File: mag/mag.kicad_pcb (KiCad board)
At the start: 4 copper layers, 87 x 51 mm, 77 parts, among them K1 Кнопка_KLS7-TS5401-1.35-250-T, K2 Кнопка_KLS7-TS5401-1.35-250-T, X1 отверстие_под_пайку, X2 отверстие_под_пайку, X3 отверстие_под_пайку, X4 отверстие_под_пайку

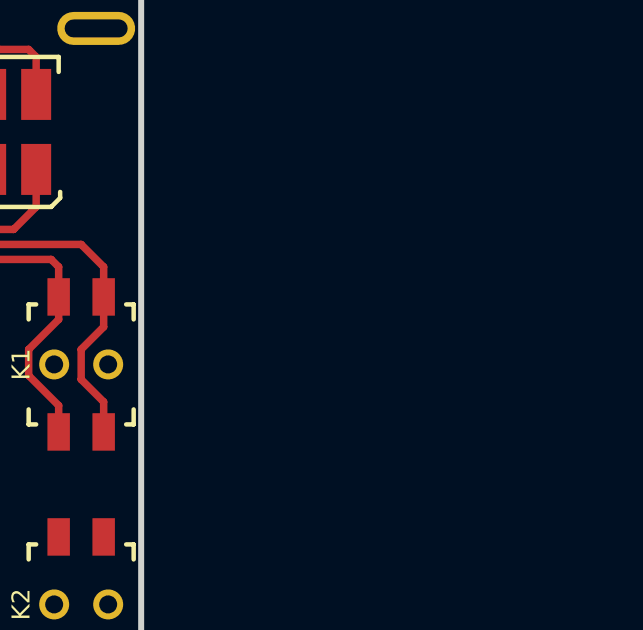
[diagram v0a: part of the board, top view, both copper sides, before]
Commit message: вынесен, но не подключен LDO на 2,5В
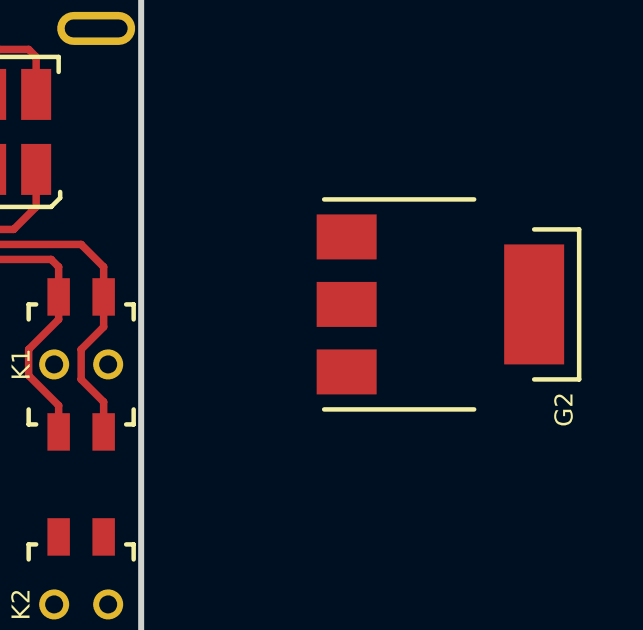
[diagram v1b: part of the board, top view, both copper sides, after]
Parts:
- added G2: Микросхема*LDO*IN8V*OUT2V5*1,2A*SOT-223, N_VD_HL:Транзистор_NPN_SOT223_pnp, F.Cu at (187.0, 87.8)

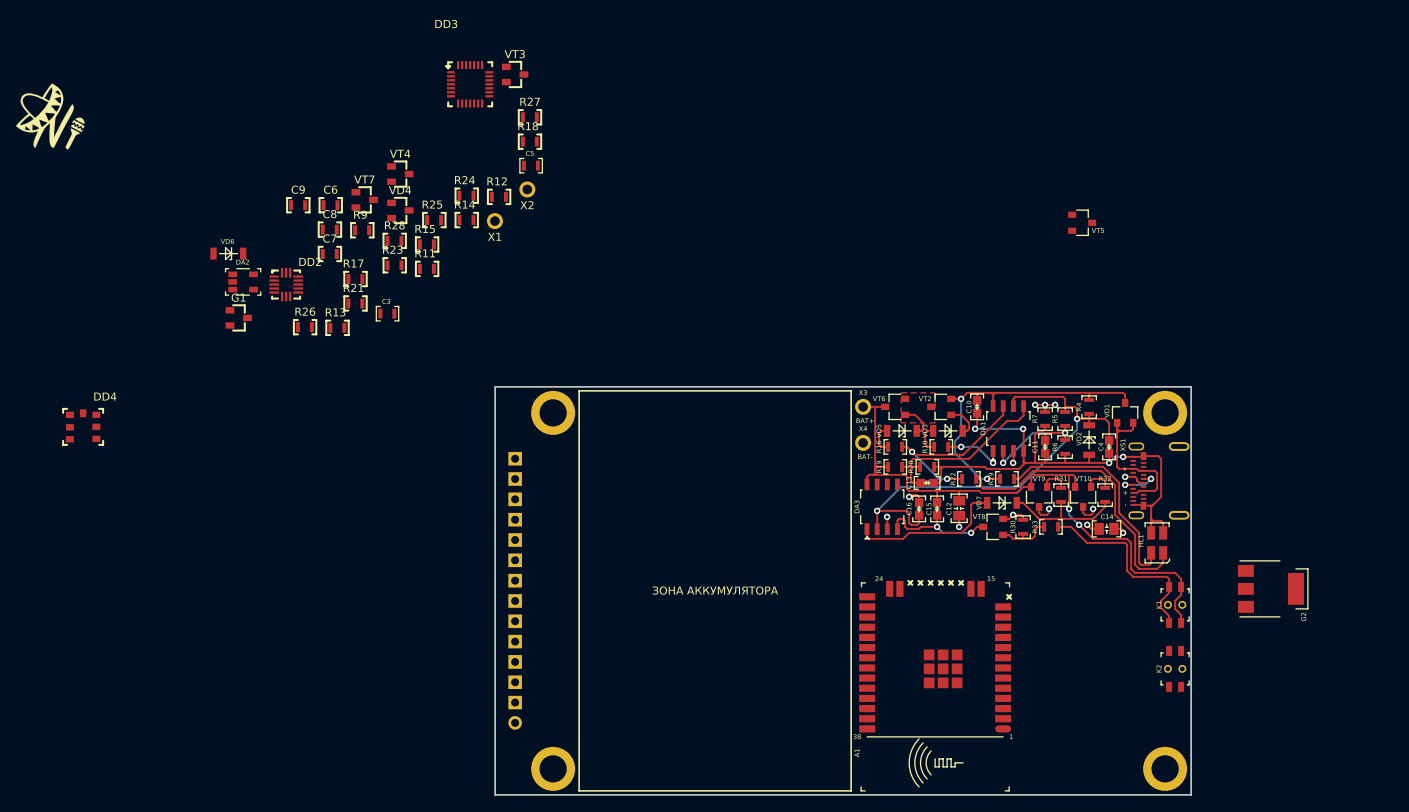
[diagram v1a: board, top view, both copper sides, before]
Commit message: схема включения 2.5В по кнопке
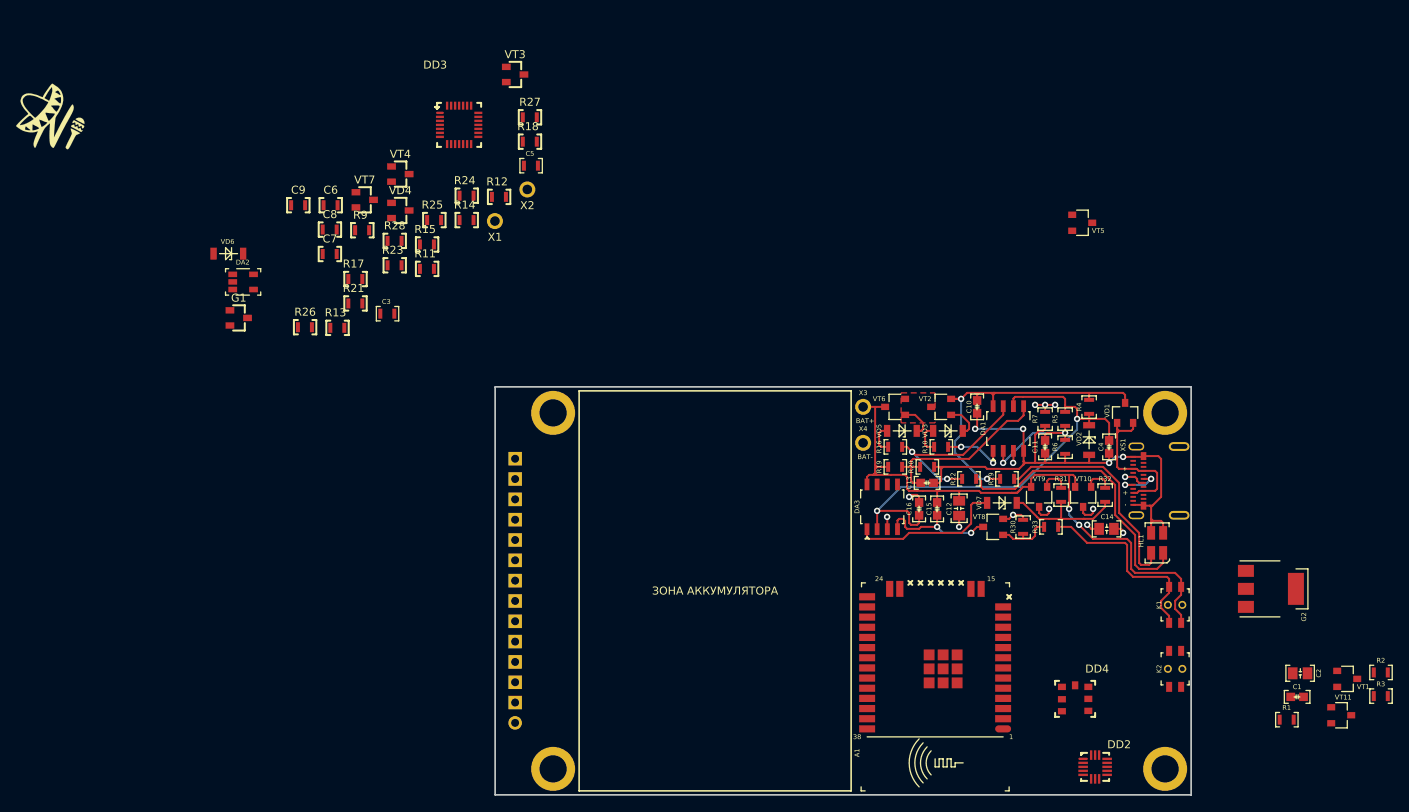
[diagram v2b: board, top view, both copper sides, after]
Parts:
- added C1: Конденсатор*0,1мкФ*25В*0603, N_RLC:Конденсатор_SMD_IEC_0603, F.Cu at (190.2, 101.2)
- added C2: Конденсатор*10мкФ*16В*0805, N_RLC:Конденсатор_SMD_IEC_0805, F.Cu at (189.7, 98.3)
- added R1: Резистор*1кОм*0603, N_RLC:Резистор_SMD_0603_0,065_Вт_pnp, F.Cu at (188.9, 104.1)
- added R2: Резистор*10кОм*0603, N_RLC:Резистор_SMD_0603_0,065_Вт_pnp, F.Cu at (200.7, 98.2)
- added R3: Резистор*1кОм*0603, N_RLC:Резистор_SMD_0603_0,065_Вт_pnp, F.Cu at (200.7, 101.2)
- added VT1: Транзистор*pnp*0,5А*45В*SOT23, N_VD_HL:Корпус_КТ-46, F.Cu at (196.5, 99.0)
- added VT11: Транзистор_полевой_N-канальный_КП526А9, MOTOR_VD_VT_HL:Корпус_КТ-46, F.Cu at (195.8, 103.5)
- moved DD4 128.6 mm to (162.5, 100.0)
- moved DD2 117.7 mm to (165.0, 110.0)
- moved DD3 5.26 mm to (83.0, 27.2)
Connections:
- net Net-(K1-Pad1) renamed /TURN
- G2 pad 1: Net-(G2-Pad1) -> GND
- G2 pad 2: Net-(G2-Pad2) -> /2V5
- G2 pad 4: Net-(G2-Pad4) -> /2V5

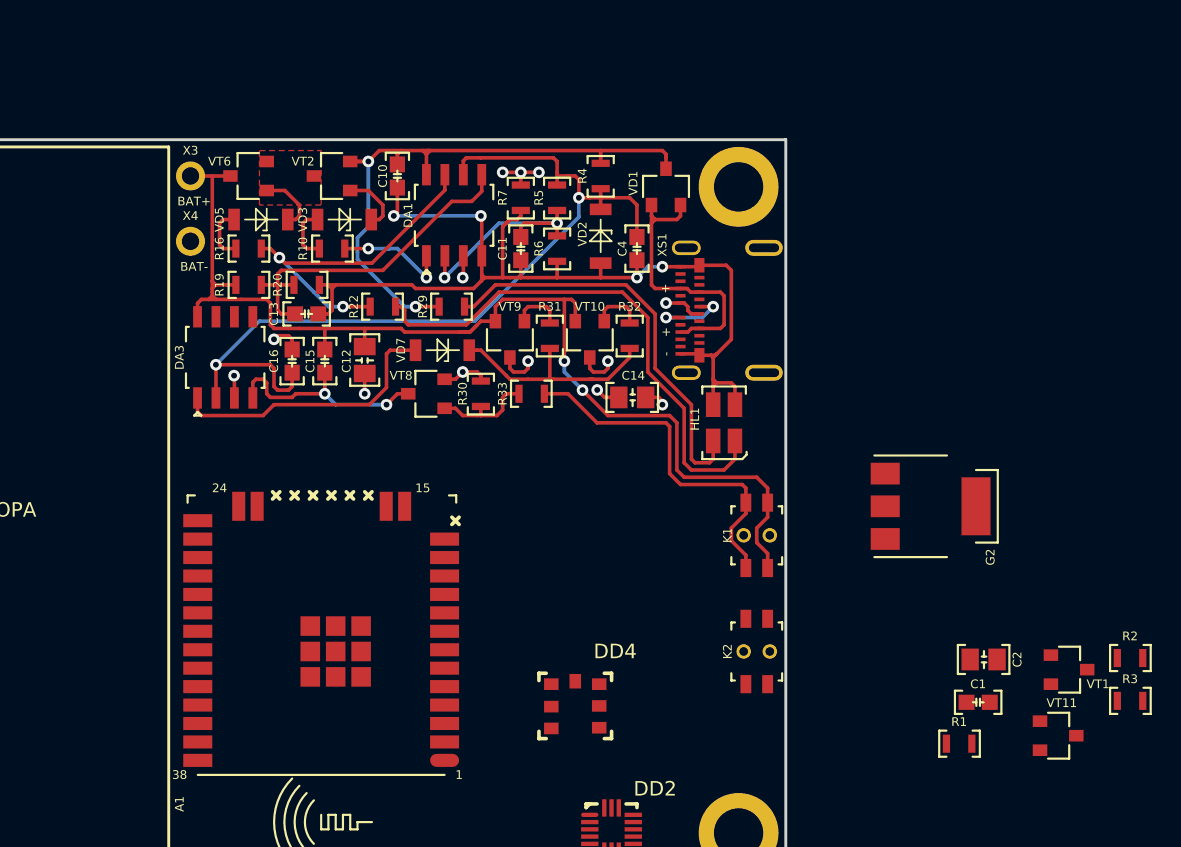
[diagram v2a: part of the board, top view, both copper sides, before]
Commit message: инициирована замена транзисторов pnp на p-канальные
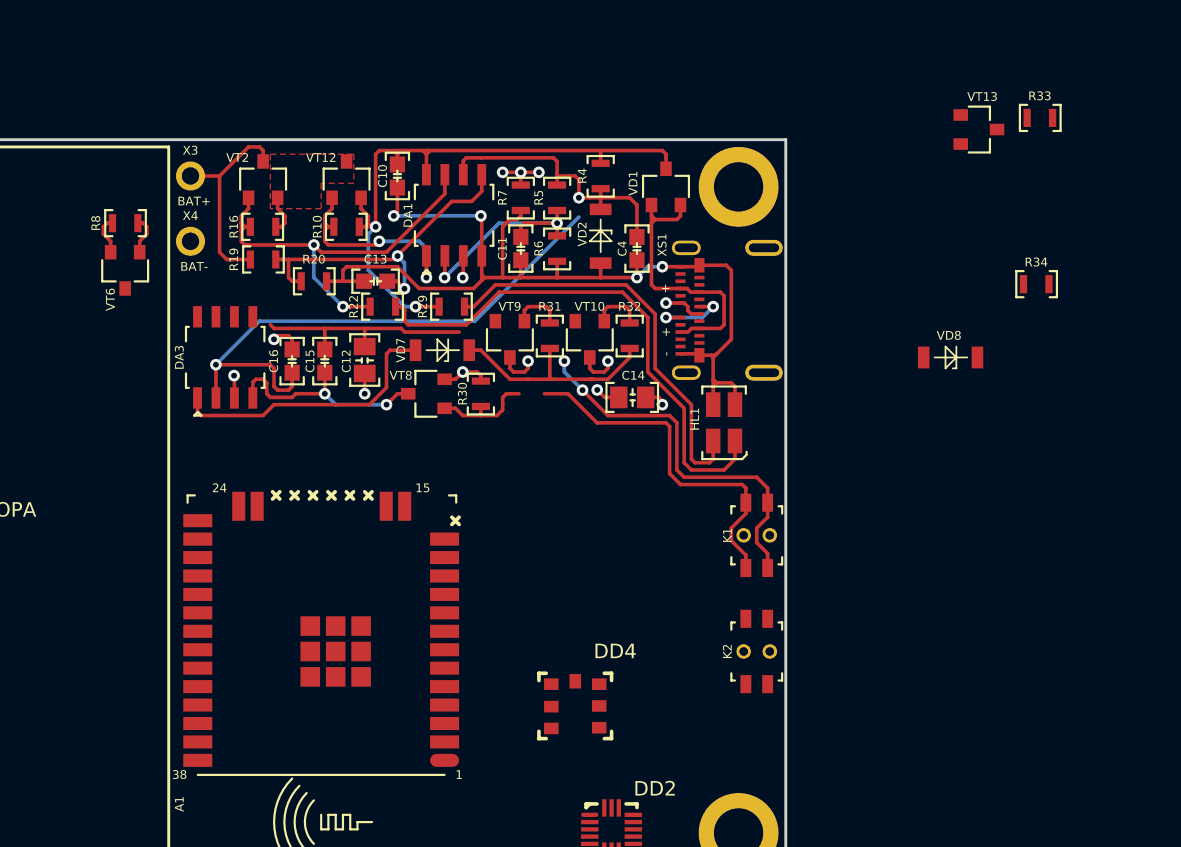
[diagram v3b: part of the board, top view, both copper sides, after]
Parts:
- removed C1: Конденсатор*0,1мкФ*25В*0603, N_RLC:Конденсатор_SMD_IEC_0603
- removed C2: Конденсатор*10мкФ*16В*0805, N_RLC:Конденсатор_SMD_IEC_0805
- removed G2: Микросхема*LDO*IN8V*OUT2V5*1,2A*SOT-223, N_VD_HL:Транзистор_NPN_SOT223_pnp
- removed R1, R3: Резистор*1кОм*0603, N_RLC:Резистор_SMD_0603_0,065_Вт_pnp
- removed R2: Резистор*10кОм*0603, N_RLC:Резистор_SMD_0603_0,065_Вт_pnp
- removed VD3, VD5: Стабилитрон*3,3В*SOD80, N_VD_HL:SOD-80
- removed VT1: Транзистор*pnp*0,5А*45В*SOT23, N_VD_HL:Корпус_КТ-46
- removed VT11: Транзистор_полевой_N-канальный_КП526А9, MOTOR_VD_VT_HL:Корпус_КТ-46
- added R34: Резистор*1кОм*0603, N_RLC:Резистор_SMD_0603_0,065_Вт_pnp, F.Cu at (194.2, 72.5)
- added R8: Резистор*1кОм*0603, N_RLC:Резистор_SMD_0603_0,065_Вт_pnp, F.Cu at (131.5, 68.2)
- added VD8: Стабилитрон*2,4В*SOD80, N_VD_HL:SOD-80, F.Cu at (186.5, 77.5)
- added VT12: Транзистор_полевой_P-канал(IRLML2246TRPBF), N_VD_HL:Корпус_КТ-46, F.Cu at (146.8, 65.2)
- added VT13: Транзистор_полевой_N-канальный_КП526А9, MOTOR_VD_VT_HL:Корпус_КТ-46, F.Cu at (190.3, 61.8)
- R16, R33: value Резистор*1кОм*0603 -> Резистор*10кОм*0603
- R19: value Резистор*2,4кОм*0603 -> Резистор*7,5кОм*0603
- R20: value Резистор*10кОм*0603 -> Резистор*11кОм*0603
- VD2, VD7: value Стабилитрон*3,3В*SOD80 -> Стабилитрон*2,4В*SOD80
- VT2, VT6: value Транзистор*pnp*0,5А*45В*SOT23 -> Транзистор_полевой_P-канал(IRLML2246TRPBF)
- moved R33 39.8 mm to (194.5, 61.0), turned to 0 degrees
- moved VT6 10.7 mm to (131.5, 71.5), turned to 270 degrees
- moved C13 5.26 mm to (148.8, 72.2), turned to 180 degrees
- moved VT2 4.76 mm to (141.0, 65.2), turned to 90 degrees
- moved R19 2.02 mm to (141.0, 70.8)
- moved R10 1.80 mm to (146.8, 68.5), turned to 180 degrees
- moved R16 1.80 mm to (141.0, 68.5), turned to 180 degrees
- moved R20 0.56 mm to (144.5, 72.2)
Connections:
- net /REF-0V1 renamed /REF-0V22
- C12 pad 1: /max4V1 -> /max4V
- C15 pad 1: /max4V1 -> /VBAT
- C15 pad 2: /COM -> Net-(C15-Pad2)
- C4 pad 1: /REF-3V3 -> /REF-2V4
- DA1 pad 6: /REF-3V3 -> /REF-2V4
- DA3 pad 4: /COM -> GND
- DA3 pad 8: /max4V1 -> /VBAT
- K1 pad 1: /TURN -> /BUTT-TURN
- K1 pad 2: /TURN -> /BUTT-TURN
- K1 pad 3: /max4V1 -> /max4V
- K1 pad 4: /max4V1 -> /max4V
- R10 pad 1: Net-(R10-Pad1) -> 5V
- R16 pad 1: Net-(R16-Pad1) -> /max0.22A
- R19 pad 1: /max4V1 -> /max4V
- R30 pad 2: Net-(R30-Pad2) -> /BUTT-TURN
- R33 pad 1: /TURN -> GND
- R33 pad 2: Net-(R30-Pad2) -> /ESP-TURN
- R4 pad 2: /REF-3V3 -> /REF-2V4
- R5 pad 1: /REF-3V3 -> /REF-2V4
- VD2 pad 2: /REF-3V3 -> /REF-2V4
- VT10 pad 2: /max4V1 -> Net-(VT10-Pad2)
- VT2 pad 1: Net-(VD3-Pad2) -> /VOL-DIRECT
- VT2 pad 2: 5V -> /max0.22A
- VT2 pad 3: /max0.3A -> /max4V
- VT6 pad 1: Net-(VD5-Pad2) -> /DIRECT
- VT6 pad 2: /max0.3A -> /max4V
- VT6 pad 3: /max4V1 -> /VBAT
- VT8 pad 1: Net-(R30-Pad2) -> /BUTT-TURN
- VT8 pad 3: /COM -> /DIRECT
- VT9 pad 2: /max4V1 -> Net-(VT10-Pad2)
- X3 pad 1: /max4V1 -> /max4V
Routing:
- net /max4V1: track 80.0 -> 0.00 mm, vias 2 -> 0
- net /max4V: track 0.00 -> 58.9 mm, vias 0 -> 2
- net /BUTT-TURN: track 0.00 -> 31.9 mm
- net /TURN: track 24.8 -> 0.00 mm
- net /REF-3V3: track 60.5 -> 39.3 mm, vias 2 -> 1
- net /REF-2V4: track 0.00 -> 19.9 mm, vias 0 -> 1
- net Net-(R30-Pad2): track 7.08 -> 0.00 mm
- net /CUR-DIRECT: track 8.20 -> 15.2 mm
- net /VOL-DIRECT: track 23.9 -> 28.6 mm
- net Net-(VD5-Pad2): track 4.32 -> 0.00 mm
- net Net-(VD3-Pad2): track 4.32 -> 0.00 mm
- net Net-(R16-Pad1): track 3.83 -> 0.00 mm
- net Net-(R10-Pad1): track 3.83 -> 0.00 mm
- net /max0.22A: track 0.00 -> 2.69 mm
- net /DIRECT: track 0.00 -> 2.69 mm
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- added copper zone on F.Cu, net /max0.22A
- removed copper zone on F.Cu, net /max0.3A
